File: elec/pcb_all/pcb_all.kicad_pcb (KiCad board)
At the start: 2 copper layers, 59.2 x 116.5 mm, 80 parts, among them IC1 TPS629203QDRLRQ1, IC2 AP63203WU-7, IC3 BQ25176MDSGR, IC4 TPS61023DRLR, IC5 BMP390, IC6 LSM6DSLTR, J1 Conn_01x02, J2 Conn_01x07, Q1 CSD16301Q2, Q2 CSD16301Q2, Q3 IRLML6344TRPBF, U1 BQ29700DSER, U2 Xiao_ESP32-C3

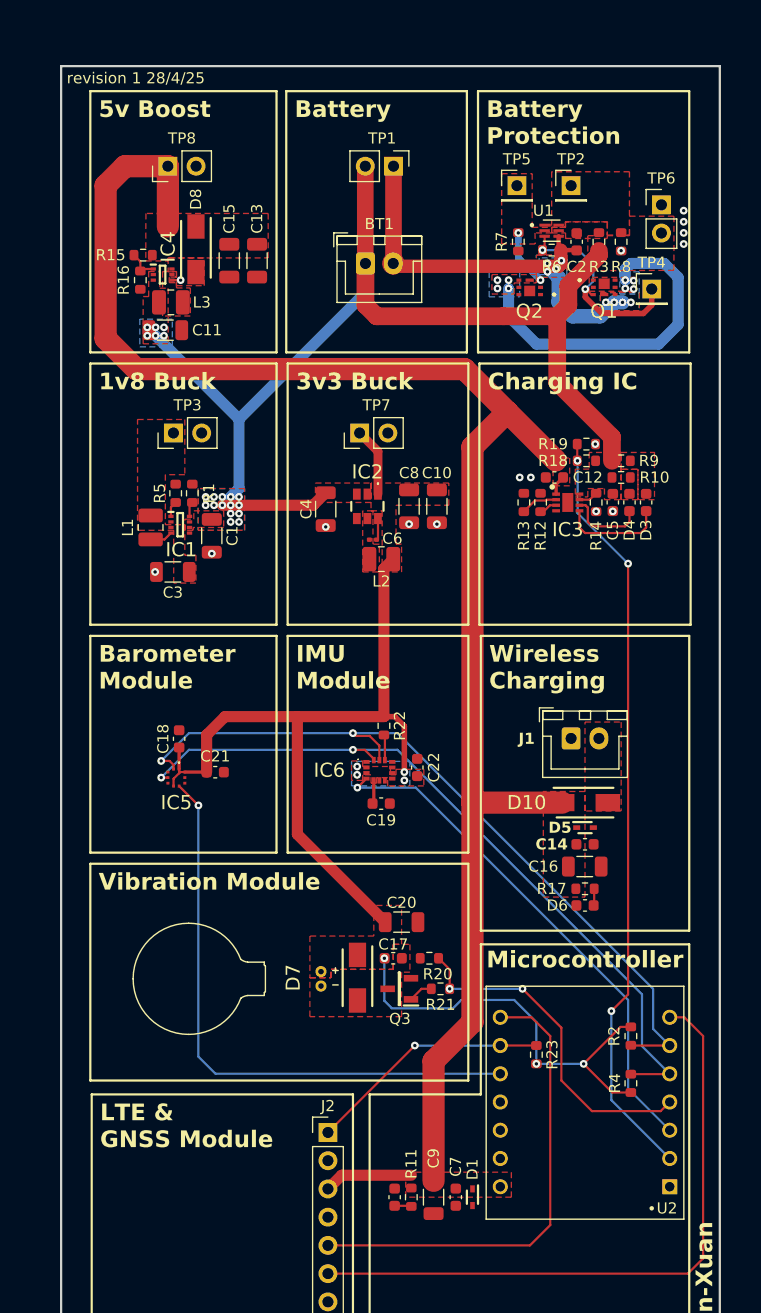
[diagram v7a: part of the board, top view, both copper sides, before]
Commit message: added lcsc numbers for all components except resistors
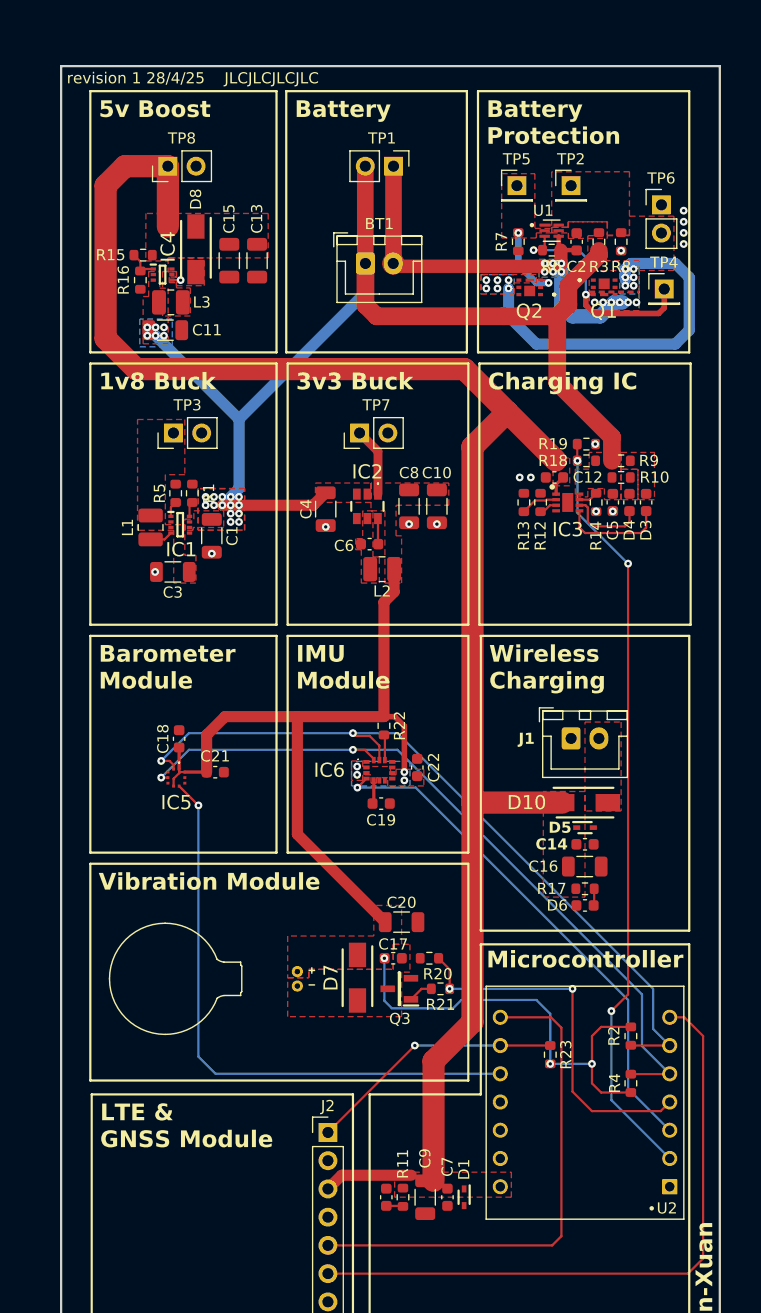
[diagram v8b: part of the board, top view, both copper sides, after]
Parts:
- C6: footprint Capacitor_SMD:C_0201_0603Metric -> Capacitor_SMD:C_0603_1608Metric
- moved B1 2.12 mm to (124.1, 132.8)
- moved R23 1.25 mm to (158.8, 139.7)
- moved TP4 1.13 mm to (169.0, 70.8)
- moved L2 0.90 mm to (143.6, 96.0)
- moved C7 0.75 mm to (149.5, 152.5)
- moved C9 0.75 mm to (147.5, 152.5)
- moved D1 0.75 mm to (151.0, 152.5)
- moved D2 0.75 mm to (144.0, 152.5)
- moved R11 0.75 mm to (145.5, 152.5)
- moved C6 0.50 mm to (142.5, 93.8)
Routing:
- net /TX (SIM7600G-H): track 43.0 -> 46.0 mm
- net /PWM (Vibration): track 30.6 -> 33.3 mm
- net Net-(Q1-G): track 18.9 -> 21.4 mm
- net Net-(Q1-D): track 30.2 -> 32.5 mm, vias 8 -> 12
- net Net-(Q2-G): track 5.08 -> 7.10 mm
- net +3V3: track 115.0 -> 116.3 mm
- net /SLEEP (SIM7600G-H): track 22.0 -> 23.2 mm
- net Net-(BT1--): track 38.4 -> 37.6 mm, vias 8 -> 12
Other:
- board text added: "revision 1 28/4/25 JLCJLCJLCJLC"
- board text removed: "revision 1 28/4/25"
